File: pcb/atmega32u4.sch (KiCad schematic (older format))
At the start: 10 parts

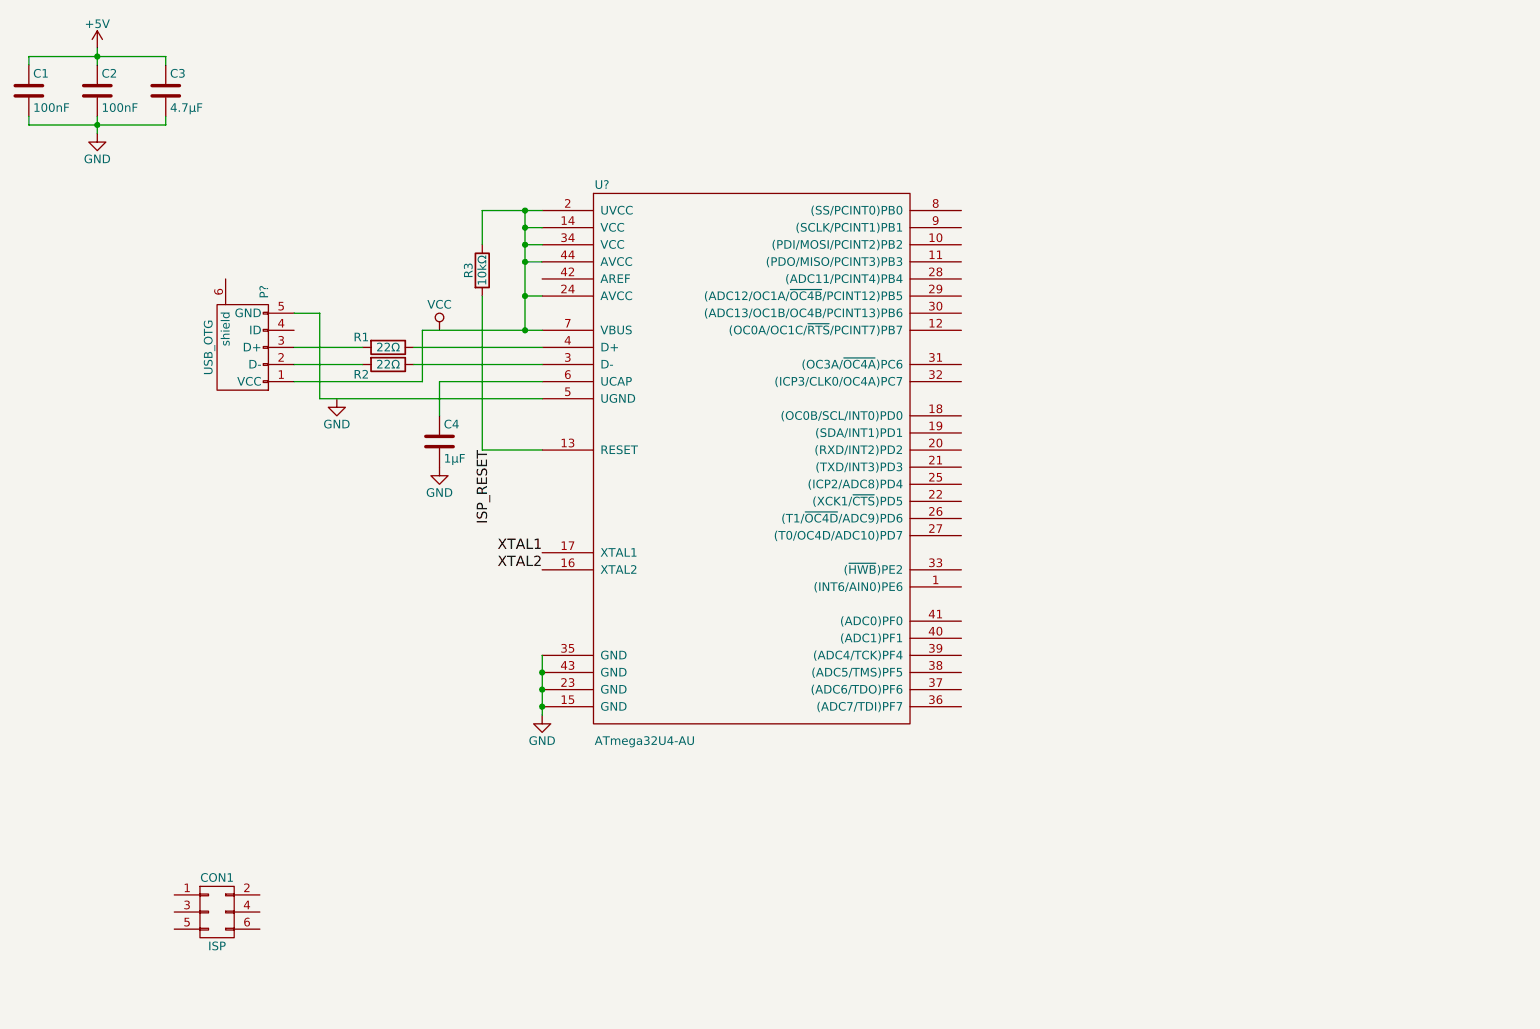
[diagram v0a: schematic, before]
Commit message: Add crystal, connectors
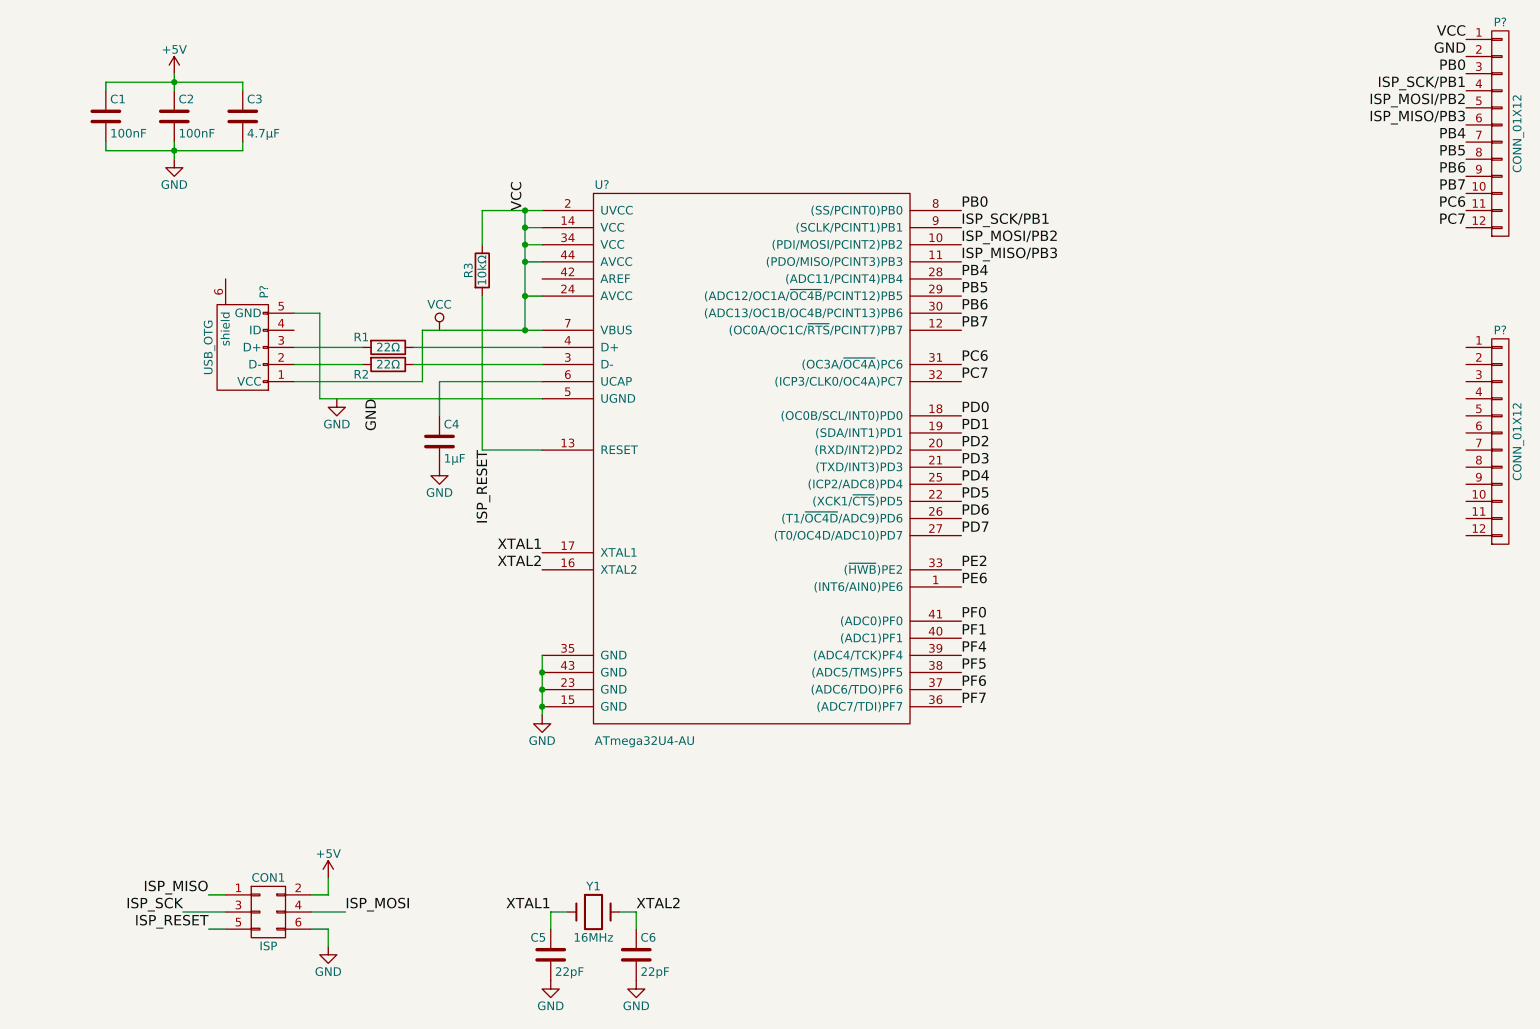
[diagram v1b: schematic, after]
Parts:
- added C5 (x2): 22pF, symbol C
- added P? (x2): CONN_01X12, symbol CONN_01X12
- added Y1: 16MHz, symbol Crystal
- gave numbers to parts that had none: 1
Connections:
- net +5V: now also CON1.2 (P2)
- net GND: now also CON1.6 (P6), P?.5 (GND), U?.5 (UGND), C5.2, C5.2, P?.2 (P2)
- net ISP_RESET: now also CON1.5 (P5)
- net VCC: now also P?.1 (VCC), R3.1, U?.14 (VCC), U?.2 (UVCC), U?.24 (AVCC), U?.34 (VCC), U?.44 (AVCC), U?.7 (VBUS), P?.1 (P1)
- net XTAL1: now also C5.1, Y1.1
- net XTAL2: now also C5.1, Y1.2
- net PE6: now reaches U?.1 ((INT6/AIN0)PE6)
- net ISP_MOSI/PB2: now reaches U?.10 ((PDI/MOSI/PCINT2)PB2)
- net ISP_MOSI/PB2: now also P?.5 (P5)
- net ISP_MISO/PB3: now reaches U?.11 ((PDO/MISO/PCINT3)PB3)
- net ISP_MISO/PB3: now also P?.6 (P6)
- net PB7: now reaches U?.12 ((OC0A/OC1C/~RTS~/PCINT7)PB7)
- net PB7: now also P?.10 (P10)
- net PD0: now reaches U?.18 ((OC0B/SCL/INT0)PD0)
- net PD1: now reaches U?.19 ((SDA/INT1)PD1)
- net PD2: now reaches U?.20 ((RXD/INT2)PD2)
- net PD3: now reaches U?.21 ((TXD/INT3)PD3)
- net PD5: now reaches U?.22 ((XCK1/~CTS~)PD5)
- net PD4: now reaches U?.25 ((ICP2/ADC8)PD4)
- net PD6: now reaches U?.26 ((T1/~OC4D~/ADC9)PD6)
- net PD7: now reaches U?.27 ((T0/OC4D/ADC10)PD7)
- net PB4: now reaches U?.28 ((ADC11/PCINT4)PB4)
- net PB4: now also P?.7 (P7)
- net PB5: now reaches U?.29 ((ADC12/OC1A/~OC4B~/PCINT12)PB5)
- net PB5: now also P?.8 (P8)
- net PB6: now reaches U?.30 ((ADC13/OC1B/OC4B/PCINT13)PB6)
- net PB6: now also P?.9 (P9)
- net PC6: now reaches U?.31 ((OC3A/~OC4A~)PC6)
- net PC6: now also P?.11 (P11)
- net PC7: now reaches U?.32 ((ICP3/CLK0/OC4A)PC7)
- net PC7: now also P?.12 (P12)
- net PE2: now reaches U?.33 ((~HWB~)PE2)
- net PF7: now reaches U?.36 ((ADC7/TDI)PF7)
- net PF6: now reaches U?.37 ((ADC6/TDO)PF6)
- net PF5: now reaches U?.38 ((ADC5/TMS)PF5)
- net PF4: now reaches U?.39 ((ADC4/TCK)PF4)
- net PF1: now reaches U?.40 ((ADC1)PF1)
- net PF0: now reaches U?.41 ((ADC0)PF0)
- net PB0: now reaches U?.8 ((SS/PCINT0)PB0)
- net PB0: now also P?.3 (P3)
- net ISP_SCK/PB1: now reaches U?.9 ((SCLK/PCINT1)PB1)
- net ISP_SCK/PB1: now also P?.4 (P4)
- net ISP_MISO: now reaches CON1.1 (P1)
- net ISP_SCK: now reaches CON1.3 (P3)
- net ISP_MOSI: now reaches CON1.4 (P4)
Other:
- moved on the sheet: C1, C2, C3, CON1

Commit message: Complete schematic
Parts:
- removed P? (x2): CONN_01X12, symbol CONN_01X12
- added P1, P2: CONN_01X14, symbol CONN_01X14
- gave numbers to parts that had none: 2
- renumbered C5 to C6
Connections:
- net GND: now also P1.2 (P2), P2.1 (P1), P2.2 (P2)
- net ISP_MISO/PB3: now also P1.6 (P6)
- net ISP_MOSI/PB2: now also P1.5 (P5)
- net ISP_SCK/PB1: now also P1.4 (P4)
- net PB0: now also P1.3 (P3)
- net PB4: now also P1.7 (P7)
- net PB5: now also P1.8 (P8)
- net PB6: now also P1.9 (P9)
- net PB7: now also P1.10 (P10)
- net PC6: now also P1.11 (P11)
- net PC7: now also P1.12 (P12)
- net PD0: now also P2.3 (P3)
- net PD1: now also P2.4 (P4)
- net PD2: now also P2.5 (P5)
- net PD3: now also P2.6 (P6)
- net PD4: now also P2.7 (P7)
- net PD5: now also P2.8 (P8)
- net PD6: now also P2.9 (P9)
- net PD7: now also P2.10 (P10)
- net PF0: now also P1.13 (P13)
- net PF1: now also P1.14 (P14)
- net PF4: now also P2.11 (P11)
- net PF5: now also P2.12 (P12)
- net PF6: now also P2.13 (P13)
- net PF7: now also P2.14 (P14)
- net VCC: now also P1.1 (P1)
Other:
- moved on the sheet: C5, C6, CON1, Y1

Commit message: Associated footprints
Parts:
- C1, C2, C3, C4, C5, C6: footprint (none) -> Capacitors_SMD:C_0805_HandSoldering
- CON1: footprint (none) -> Pin_Headers:Pin_Header_Straight_2x03
- P1, P2: footprint (none) -> Pin_Headers:Pin_Header_Straight_1x14
- P3: footprint (none) -> Connect:USB_Micro-B
- R1, R2, R3: footprint (none) -> Resistors_SMD:R_0805_HandSoldering
- U1: footprint (none) -> ATMEGA32U4-AU:QFP80P1200X1200X120-44N
- Y1: footprint (none) -> Crystals:Crystal_HC50-U_Vertical
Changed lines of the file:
@@
 F 0 "P3" H 2425 2575 50  0000 C CNN
 F 1 "USB_OTG" H 2100 2900 50  0000 C CNN
-F 2 "" V 2050 2600 50  0000 C CNN
+F 2 "Connect:USB_Micro-B" V 2050 2600 50  0001 C CNN
 F 3 "" V 2050 2600 50  0000 C CNN
 	1    2100 2700
@@
 $EndComp
 $Comp
-L GND #PWR6
+L GND #PWR01
 U 1 1 57DFD5E2
 P 3850 4850
-F 0 "#PWR6" H 3850 4600 50  0001 C CNN
+F 0 "#PWR01" H 3850 4600 50  0001 C CNN
 F 1 "GND" H 3850 4700 50  0000 C CNN
 F 2 "" H 3850 4850 50  0000 C CNN
@@
 F 0 "R2" V 3009 2643 50  0000 C CNN
 F 1 "22Ω" V 2950 2800 50  0000 C CNN
-F 2 "" V 2880 2800 50  0000 C CNN
+F 2 "Resistors_SMD:R_0805_HandSoldering" V 2880 2800 50  0001 C CNN
 F 3 "" H 2950 2800 50  0000 C CNN
 	1    2950 2800
@@
 F 0 "R1" V 2891 2543 50  0000 C CNN
 F 1 "22Ω" V 2950 2700 50  0000 C CNN
-F 2 "" V 2880 2700 50  0000 C CNN
+F 2 "Resistors_SMD:R_0805_HandSoldering" V 2880 2700 50  0001 C CNN
 F 3 "" H 2950 2700 50  0000 C CNN
 	1    2950 2700
@@
 $EndComp
 $Comp
-L VCC #PWR4
+L VCC #PWR02
 U 1 1 57DFDA3E
 P 3250 2600
-F 0 "#PWR4" H 3250 2450 50  0001 C CNN
+F 0 "#PWR02" H 3250 2450 50  0001 C CNN
 F 1 "VCC" H 3250 2750 50  0000 C CNN
 F 2 "" H 3250 2600 50  0000 C CNN
@@
 F 0 "U1" H 4200 5150 50  0000 C CNN
 F 1 "ATmega32U4-AU" H 4450 1900 50  0000 C CNN
-F 2 "" H 6300 4550 50  0000 C CNN
+F 2 "ATMEGA32U4-AU:QFP80P1200X1200X120-44N" H 6300 4550 50  0001 C CNN
 F 3 "" H 6300 4550 50  0000 C CNN
 	1    5100 3450
@@
 $EndComp
 $Comp
-L GND #PWR3
+L GND #PWR03
 U 1 1 57DFDBDF
 P 2650 3000
-F 0 "#PWR3" H 2650 2750 50  0001 C CNN
+F 0 "#PWR03" H 2650 2750 50  0001 C CNN
 F 1 "GND" H 2650 2850 50  0000 C CNN
 F 2 "" H 2650 3000 50  0000 C CNN
@@
 F 0 "C4" H 3275 3350 50  0000 L CNN
 F 1 "1µF" H 3275 3150 50  0000 L CNN
-F 2 "" H 3288 3100 50  0000 C CNN
+F 2 "Capacitors_SMD:C_0805_HandSoldering" H 3288 3100 50  0001 C CNN
 F 3 "" H 3250 3250 50  0000 C CNN
 	1    3250 3250
@@
 $EndComp
 $Comp
-L GND #PWR5
+L GND #PWR04
 U 1 1 57DFDCB3
 P 3250 3400
-F 0 "#PWR5" H 3250 3150 50  0001 C CNN
+F 0 "#PWR04" H 3250 3150 50  0001 C CNN
 F 1 "GND" H 3250 3250 50  0000 C CNN
 F 2 "" H 3250 3400 50  0000 C CNN
@@
 $EndComp
 $Comp
-L +5V #PWR1
+L +5V #PWR05
 U 1 1 57DFDE44
 P 1700 1100
-F 0 "#PWR1" H 1700 950 50  0001 C CNN
+F 0 "#PWR05" H 1700 950 50  0001 C CNN
 F 1 "+5V" H 1700 1240 50  0000 C CNN
 F 2 "" H 1700 1100 50  0000 C CNN
@@
 F 0 "C1" H 1325 1450 50  0000 L CNN
 F 1 "100nF" H 1325 1250 50  0000 L CNN
-F 2 "" H 1338 1200 50  0000 C CNN
+F 2 "Capacitors_SMD:C_0805_HandSoldering" H 1338 1200 50  0001 C CNN
 F 3 "" H 1300 1350 50  0000 C CNN
 	1    1300 1350
@@
 F 0 "C2" H 1725 1450 50  0000 L CNN
 F 1 "100nF" H 1725 1250 50  0000 L CNN
-F 2 "" H 1738 1200 50  0000 C CNN
+F 2 "Capacitors_SMD:C_0805_HandSoldering" H 1738 1200 50  0001 C CNN
 F 3 "" H 1700 1350 50  0000 C CNN
 	1    1700 1350
@@
 F 0 "C3" H 2125 1450 50  0000 L CNN
 F 1 "4.7µF" H 2125 1250 50  0000 L CNN
-F 2 "" H 2138 1200 50  0000 C CNN
+F 2 "Capacitors_SMD:C_0805_HandSoldering" H 2138 1200 50  0001 C CNN
 F 3 "" H 2100 1350 50  0000 C CNN
 	1    2100 1350
@@
 $EndComp
 $Comp
-L GND #PWR2
+L GND #PWR06
 U 1 1 57DFE11A
 P 1700 1600
-F 0 "#PWR2" H 1700 1350 50  0001 C CNN
+F 0 "#PWR06" H 1700 1350 50  0001 C CNN
 F 1 "GND" H 1700 1450 50  0000 C CNN
 F 2 "" H 1700 1600 50  0000 C CNN
@@
 F 0 "R3" V 3420 2250 50  0000 C CNN
 F 1 "10kΩ" V 3500 2250 50  0000 C CNN
-F 2 "" V 3430 2250 50  0000 C CNN
+F 2 "Resistors_SMD:R_0805_HandSoldering" V 3430 2250 50  0001 C CNN
 F 3 "" H 3500 2250 50  0000 C CNN
 	1    3500 2250
@@
 Connection ~ 3750 2400
 Wire Wire Line
-	3500 1900 3750 1900
-Wire Wire Line
-	3750 1900 3850 1900
+	3500 1900 3850 1900
 Wire Wire Line
 	3500 3300 3500 2400
@@
 	1300 1550 1300 1500
 Wire Wire Line
-	1300 1550 1700 1550
-Wire Wire Line
-	1700 1550 2100 1550
-Wire Wire Line
-	1700 1500 1700 1550
-Wire Wire Line
-	1700 1550 1700 1600
+	1300 1550 2100 1550
+Wire Wire Line
+	1700 1500 1700 1600
 Wire Wire Line
 	2100 1150 2100 1200
@@
 	1300 1150 1300 1200
 Wire Wire Line
-	1300 1150 1700 1150
-Wire Wire Line
-	1700 1150 2100 1150
-Wire Wire Line
-	1700 1100 1700 1150
-Wire Wire Line
-	1700 1150 1700 1200
-Wire Wire Line
-	3850 4500 3850 4600
-Wire Wire Line
-	3850 4600 3850 4700
-Wire Wire Line
-	3850 4700 3850 4800
-Wire Wire Line
-	3850 4800 3850 4850
+	1300 1150 2100 1150
+Wire Wire Line
+	1700 1100 1700 1200
+Wire Wire Line
+	3850 4500 3850 4850
 Connection ~ 3850 4600
 Connection ~ 3850 4700
@@
 	2400 2800 2800 2800
 Wire Wire Line
-	3150 2600 3750 2600
-Wire Wire Line
-	3750 2600 3850 2600
+	3150 2600 3850 2600
 Wire Wire Line
 	3150 2600 3150 2900
@@
 	3150 2900 2400 2900
 Wire Wire Line
-	3850 2400 3750 2400
-Wire Wire Line
-	3750 1900 3750 2000
-Wire Wire Line
-	3750 2000 3750 2100
-Wire Wire Line
-	3750 2100 3750 2200
-Wire Wire Line
-	3750 2200 3750 2400
-Wire Wire Line
-	3750 2400 3750 2600
+	3750 2400 3850 2400
+Wire Wire Line
+	3750 1900 3750 2600
 Connection ~ 3750 2600
 Wire Wire Line
@@
 F 0 "CON1" H 3650 6100 50  0000 C CNN
 F 1 "ISP" H 3650 5700 50  0000 C CNN
-F 2 "" H 3650 4700 50  0000 C CNN
+F 2 "Pin_Headers:Pin_Header_Straight_2x03" H 3650 4700 50  0001 C CNN
 F 3 "" H 3650 4700 50  0000 C CNN
 	1    3650 5900
@@
 	4000 5800 4000 5700
 $Comp
-L +5V #PWR7
+L +5V #PWR07
 U 1 1 57DFE2FD
 P 4000 5700
-F 0 "#PWR7" H 4000 5550 50  0001 C CNN
+F 0 "#PWR07" H 4000 5550 50  0001 C CNN
 F 1 "+5V" H 4000 5840 50  0000 C CNN
 F 2 "" H 4000 5700 50  0000 C CNN
@@
 	4000 6000 4000 6100
 $Comp
-L GND #PWR8
+L GND #PWR08
 U 1 1 57DFE368
 P 4000 6100
-F 0 "#PWR8" H 4000 5850 50  0001 C CNN
+F 0 "#PWR08" H 4000 5850 50  0001 C CNN
 F 1 "GND" H 4000 5950 50  0000 C CNN
 F 2 "" H 4000 6100 50  0000 C CNN
@@
 F 0 "Y1" H 5550 6050 50  0000 C CNN
 F 1 "16MHz" H 5550 5750 50  0000 C CNN
-F 2 "" H 5550 5900 50  0000 C CNN
+F 2 "Crystals:Crystal_HC50-U_Vertical" H 5550 5900 50  0001 C CNN
 F 3 "" H 5550 5900 50  0000 C CNN
 	1    5550 5900
@@
 F 0 "C6" H 5825 6250 50  0000 L CNN
 F 1 "22pF" H 5825 6050 50  0000 L CNN
-F 2 "" H 5838 6000 50  0000 C CNN
+F 2 "Capacitors_SMD:C_0805_HandSoldering" H 5838 6000 50  0001 C CNN
 F 3 "" H 5800 6150 50  0000 C CNN
 	1    5800 6150
@@
 F 0 "C5" H 5182 6250 50  0000 L CNN
 F 1 "22pF" H 5325 6050 50  0000 L CNN
-F 2 "" H 5338 6000 50  0000 C CNN
+F 2 "Capacitors_SMD:C_0805_HandSoldering" H 5338 6000 50  0001 C CNN
 F 3 "" H 5300 6150 50  0000 C CNN
 	1    5300 6150
@@
 XTAL1
 $Comp
-L GND #PWR9
+L GND #PWR09
 U 1 1 57DFEE60
 P 5300 6300
-F 0 "#PWR9" H 5300 6050 50  0001 C CNN
+F 0 "#PWR09" H 5300 6050 50  0001 C CNN
 F 1 "GND" H 5300 6150 50  0000 C CNN
 F 2 "" H 5300 6300 50  0000 C CNN
@@
 $EndComp
 $Comp
-L GND #PWR10
+L GND #PWR010
 U 1 1 57DFEE9B
 P 5800 6300
-F 0 "#PWR10" H 5800 6050 50  0001 C CNN
+F 0 "#PWR010" H 5800 6050 50  0001 C CNN
 F 1 "GND" H 5800 6150 50  0000 C CNN
 F 2 "" H 5800 6300 50  0000 C CNN
@@
 F 0 "P1" H 8800 3250 50  0000 C CNN
 F 1 "CONN_01X14" V 8900 2500 50  0000 C CNN
-F 2 "" H 8800 2500 50  0000 C CNN
+F 2 "Pin_Headers:Pin_Header_Straight_1x14" H 8800 2500 50  0001 C CNN
 F 3 "" H 8800 2500 50  0000 C CNN
 	1    8800 2500
@@
 F 0 "P2" H 8800 5050 50  0000 C CNN
 F 1 "CONN_01X14" V 8900 4300 50  0000 C CNN
-F 2 "" H 8800 4300 50  0000 C CNN
+F 2 "Pin_Headers:Pin_Header_Straight_1x14" H 8800 4300 50  0001 C CNN
 F 3 "" H 8800 4300 50  0000 C CNN
 	1    8800 4300

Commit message: Fix up CONN labels on schematic
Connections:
- net ISP_MISO is gone; now on net ISP_MISO/PB3: CON1.1 (P1)
- net ISP_MOSI is gone; now on net ISP_MOSI/PB2: CON1.4 (P4)
- net ISP_SCK is gone; now on net ISP_SCK/PB1: CON1.3 (P3)
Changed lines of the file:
@@
-$EndComp
-$Comp
-L VCC #PWR02
-U 1 1 57DFDA3E
-P 3250 2600
-F 0 "#PWR02" H 3250 2450 50  0001 C CNN
-F 1 "VCC" H 3250 2750 50  0000 C CNN
-F 2 "" H 3250 2600 50  0000 C CNN
-F 3 "" H 3250 2600 50  0000 C CNN
-	1    3250 2600
-	1    0    0    -1
 $EndComp
 $Comp
@@
 $EndComp
 $Comp
-L GND #PWR03
+L GND #PWR02
 U 1 1 57DFDBDF
 P 2650 3000
-F 0 "#PWR03" H 2650 2750 50  0001 C CNN
+F 0 "#PWR02" H 2650 2750 50  0001 C CNN
 F 1 "GND" H 2650 2850 50  0000 C CNN
 F 2 "" H 2650 3000 50  0000 C CNN
@@
 $EndComp
 $Comp
-L GND #PWR04
+L GND #PWR03
 U 1 1 57DFDCB3
 P 3250 3400
-F 0 "#PWR04" H 3250 3150 50  0001 C CNN
+F 0 "#PWR03" H 3250 3150 50  0001 C CNN
 F 1 "GND" H 3250 3250 50  0000 C CNN
 F 2 "" H 3250 3400 50  0000 C CNN
@@
 $EndComp
 $Comp
-L +5V #PWR05
+L +5V #PWR04
 U 1 1 57DFDE44
 P 1700 1100
-F 0 "#PWR05" H 1700 950 50  0001 C CNN
+F 0 "#PWR04" H 1700 950 50  0001 C CNN
 F 1 "+5V" H 1700 1240 50  0000 C CNN
 F 2 "" H 1700 1100 50  0000 C CNN
@@
 $EndComp
 $Comp
-L GND #PWR06
+L GND #PWR05
 U 1 1 57DFE11A
 P 1700 1600
-F 0 "#PWR06" H 1700 1350 50  0001 C CNN
+F 0 "#PWR05" H 1700 1350 50  0001 C CNN
 F 1 "GND" H 1700 1450 50  0000 C CNN
 F 2 "" H 1700 1600 50  0000 C CNN
@@
 	4000 5800 4000 5700
 $Comp
-L +5V #PWR07
+L +5V #PWR06
 U 1 1 57DFE2FD
 P 4000 5700
-F 0 "#PWR07" H 4000 5550 50  0001 C CNN
+F 0 "#PWR06" H 4000 5550 50  0001 C CNN
 F 1 "+5V" H 4000 5840 50  0000 C CNN
 F 2 "" H 4000 5700 50  0000 C CNN
@@
 	4000 6000 4000 6100
 $Comp
-L GND #PWR08
+L GND #PWR07
 U 1 1 57DFE368
 P 4000 6100
-F 0 "#PWR08" H 4000 5850 50  0001 C CNN
+F 0 "#PWR07" H 4000 5850 50  0001 C CNN
 F 1 "GND" H 4000 5950 50  0000 C CNN
 F 2 "" H 4000 6100 50  0000 C CNN
@@
 	3900 5900 4100 5900
 Text Label 4100 5900 0    60   ~ 0
-ISP_MOSI
+ISP_MOSI/PB2
 Wire Wire Line
 	3400 5900 3150 5900
 Text Label 3300 5800 2    60   ~ 0
-ISP_MISO
+ISP_MISO/PB3
 Wire Wire Line
 	3400 5800 3300 5800
 Text Label 3150 5900 2    60   ~ 0
-ISP_SCK
+ISP_SCK/PB1
 Wire Wire Line
 	3400 6000 3300 6000
@@
 XTAL1
 $Comp
-L GND #PWR09
+L GND #PWR08
 U 1 1 57DFEE60
 P 5300 6300
-F 0 "#PWR09" H 5300 6050 50  0001 C CNN
+F 0 "#PWR08" H 5300 6050 50  0001 C CNN
 F 1 "GND" H 5300 6150 50  0000 C CNN
 F 2 "" H 5300 6300 50  0000 C CNN
@@
 $EndComp
 $Comp
-L GND #PWR010
+L GND #PWR09
 U 1 1 57DFEE9B
 P 5800 6300
-F 0 "#PWR010" H 5800 6050 50  0001 C CNN
+F 0 "#PWR09" H 5800 6050 50  0001 C CNN
 F 1 "GND" H 5800 6150 50  0000 C CNN
 F 2 "" H 5800 6300 50  0000 C CNN
@@
 Text Label 8600 4950 2    60   ~ 0
 PF7
+$Comp
+L +5V #PWR010
+U 1 1 57E26C1F
+P 3250 2600
+F 0 "#PWR010" H 3250 2450 50  0001 C CNN
+F 1 "+5V" H 3250 2740 50  0000 C CNN
+F 2 "" H 3250 2600 50  0000 C CNN
+F 3 "" H 3250 2600 50  0000 C CNN
+	1    3250 2600
+	1    0    0    -1
+$EndComp
 $EndSCHEMATC

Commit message: Add outline to board
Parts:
- Y1: footprint Crystals:Crystal_HC50-U_Vertical -> Crystals:Crystal_HC49-U_Vertical
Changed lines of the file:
@@
 F 0 "Y1" H 5550 6050 50  0000 C CNN
 F 1 "16MHz" H 5550 5750 50  0000 C CNN
-F 2 "Crystals:Crystal_HC50-U_Vertical" H 5550 5900 50  0001 C CNN
+F 2 "Crystals:Crystal_HC49-U_Vertical" H 5550 5900 50  0001 C CNN
 F 3 "" H 5550 5900 50  0000 C CNN
 	1    5550 5900
